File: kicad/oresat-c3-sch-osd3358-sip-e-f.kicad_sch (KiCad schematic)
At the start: 5 parts, among them U1 OSD3358-512M-BSM

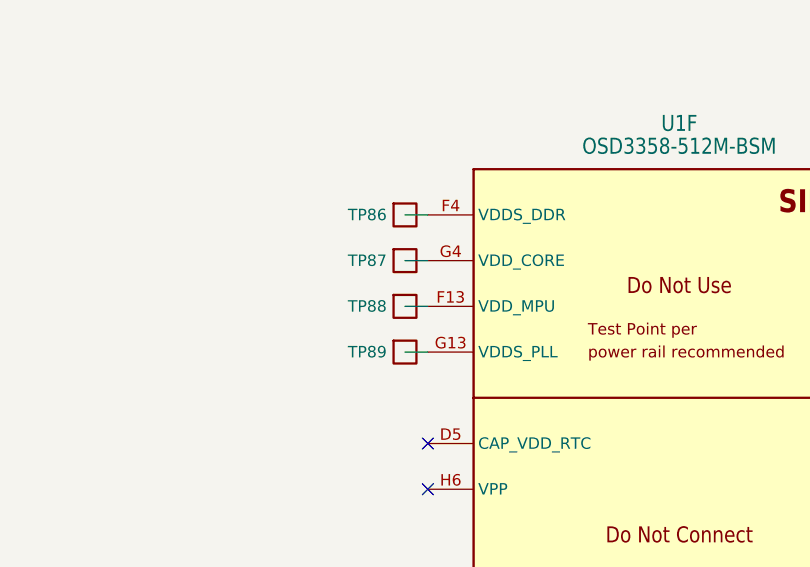
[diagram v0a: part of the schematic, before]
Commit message: Sane amount of ERC errors now; mostly library cleanups.
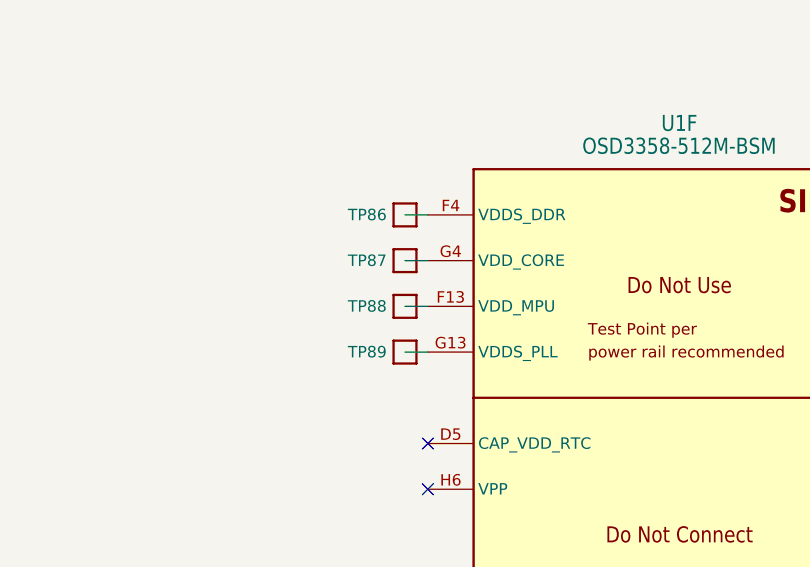
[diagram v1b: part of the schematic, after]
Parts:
- TP86, TP87, TP88, TP89: footprint OreSat-TestPoint:PAD.03X.04 -> oresat-misc:PAD.03X.04; symbol OreSat-TestPoint:Test-Point -> oresat-misc:Test-Point
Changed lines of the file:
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@@
     (effects (font (size 1.27 1.27)) (justify left bottom))
   )
-  (symbol (lib_id "OreSat-Power:GND") (at 250.19 125.73 0) (unit 1)
+  (symbol (lib_id "oresat-power:GND") (at 250.19 125.73 0) (unit 1)
     (in_bom yes) (on_board yes) (dnp no)
     (property "Reference" "#GND0172" (at 250.19 132.08 0)
@@
     )
   )
-  (symbol (lib_id "OreSat-Power:GND") (at 184.15 125.73 0) (unit 1)
+  (symbol (lib_id "oresat-power:GND") (at 184.15 125.73 0) (unit 1)
     (in_bom yes) (on_board yes) (dnp no)
     (property "Reference" "#GND0173" (at 184.15 132.08 0)
@@
     )
   )
-  (symbol (lib_id "OreSat-TestPoint:Test-Point") (at 187.96 162.56 0) (unit 1)
+  (symbol (lib_id "oresat-misc:Test-Point") (at 187.96 162.56 0) (unit 1)
     (in_bom yes) (on_board yes) (dnp no)
     (property "Reference" "TP86" (at 181.61 162.56 0)
@@
       (effects (font (size 1.27 1.27)) hide)
     )
-    (property "Footprint" "OreSat-TestPoint:PAD.03X.04" (at 187.96 160.02 0)
+    (property "Footprint" "oresat-misc:PAD.03X.04" (at 187.96 160.02 0)
       (effects (font (size 1.27 1.27)) hide)
     )
@@
     )
   )
-  (symbol (lib_id "OreSat-TestPoint:Test-Point") (at 187.96 167.64 0) (unit 1)
+  (symbol (lib_id "oresat-misc:Test-Point") (at 187.96 167.64 0) (unit 1)
     (in_bom yes) (on_board yes) (dnp no)
     (property "Reference" "TP87" (at 181.61 167.64 0)
@@
       (effects (font (size 1.27 1.27)) hide)
     )
-    (property "Footprint" "OreSat-TestPoint:PAD.03X.04" (at 187.96 165.1 0)
+    (property "Footprint" "oresat-misc:PAD.03X.04" (at 187.96 165.1 0)
       (effects (font (size 1.27 1.27)) hide)
     )
@@
     )
   )
-  (symbol (lib_id "OreSat-TestPoint:Test-Point") (at 187.96 177.8 0) (unit 1)
+  (symbol (lib_id "oresat-misc:Test-Point") (at 187.96 177.8 0) (unit 1)
     (in_bom yes) (on_board yes) (dnp no)
     (property "Reference" "TP89" (at 181.61 177.8 0)
@@
       (effects (font (size 1.27 1.27)) hide)
     )
-    (property "Footprint" "OreSat-TestPoint:PAD.03X.04" (at 187.96 175.26 0)
+    (property "Footprint" "oresat-misc:PAD.03X.04" (at 187.96 175.26 0)
       (effects (font (size 1.27 1.27)) hide)
     )
@@
     )
   )
-  (symbol (lib_id "OreSat-TestPoint:Test-Point") (at 187.96 172.72 0) (unit 1)
+  (symbol (lib_id "oresat-misc:Test-Point") (at 187.96 172.72 0) (unit 1)
     (in_bom yes) (on_board yes) (dnp no)
     (property "Reference" "TP88" (at 181.61 172.72 0)
@@
       (effects (font (size 1.27 1.27)) hide)
     )
-    (property "Footprint" "OreSat-TestPoint:PAD.03X.04" (at 187.96 170.18 0)
-      (effects (font (size 1.27 1.27)) hide)
-    )
+    (property "Footprint" "oresat-misc:PAD.03X.04" (at 187.96 170.18 0)
+      (effects (font (size 1.27 1.27)) hide)
+    )

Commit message: Big C3 cleanup with Glenn; radios off of one SPS + separate LDOs, removed lots of test 0 ohm resistors, cleaned up capacitance, and finally wired everything up to the octavo. ZERO ERC errors.
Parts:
- TP86, TP87, TP88, TP89: footprint oresat-misc:PAD.03X.04 -> TestPoint:TestPoint_Pad_D1.0mm; symbol oresat-misc:Test-Point -> oresat-misc:Test-Point-1mm-round
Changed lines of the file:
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@@
     )
   )
-  (symbol (lib_id "oresat-misc:Test-Point") (at 187.96 162.56 0) (unit 1)
+  (symbol (lib_id "oresat-misc:Test-Point-1mm-round") (at 187.96 162.56 0) (unit 1)
     (in_bom yes) (on_board yes) (dnp no)
     (property "Reference" "TP86" (at 181.61 162.56 0)
@@
       (effects (font (size 1.27 1.27)) hide)
     )
-    (property "Footprint" "oresat-misc:PAD.03X.04" (at 187.96 160.02 0)
+    (property "Footprint" "TestPoint:TestPoint_Pad_D1.0mm" (at 187.96 152.4 0)
       (effects (font (size 1.27 1.27)) hide)
     )
-    (property "Datasheet" "" (at 187.96 160.02 0)
+    (property "Datasheet" "" (at 187.96 162.56 0)
       (effects (font (size 1.27 1.27)) hide)
     )
@@
     )
   )
-  (symbol (lib_id "oresat-misc:Test-Point") (at 187.96 167.64 0) (unit 1)
+  (symbol (lib_id "oresat-misc:Test-Point-1mm-round") (at 187.96 167.64 0) (unit 1)
     (in_bom yes) (on_board yes) (dnp no)
     (property "Reference" "TP87" (at 181.61 167.64 0)
@@
       (effects (font (size 1.27 1.27)) hide)
     )
-    (property "Footprint" "oresat-misc:PAD.03X.04" (at 187.96 165.1 0)
+    (property "Footprint" "TestPoint:TestPoint_Pad_D1.0mm" (at 187.96 157.48 0)
       (effects (font (size 1.27 1.27)) hide)
     )
-    (property "Datasheet" "" (at 187.96 165.1 0)
+    (property "Datasheet" "" (at 187.96 167.64 0)
       (effects (font (size 1.27 1.27)) hide)
     )
@@
     )
   )
-  (symbol (lib_id "oresat-misc:Test-Point") (at 187.96 177.8 0) (unit 1)
+  (symbol (lib_id "oresat-misc:Test-Point-1mm-round") (at 187.96 177.8 0) (unit 1)
     (in_bom yes) (on_board yes) (dnp no)
     (property "Reference" "TP89" (at 181.61 177.8 0)
@@
       (effects (font (size 1.27 1.27)) hide)
     )
-    (property "Footprint" "oresat-misc:PAD.03X.04" (at 187.96 175.26 0)
+    (property "Footprint" "TestPoint:TestPoint_Pad_D1.0mm" (at 187.96 167.64 0)
       (effects (font (size 1.27 1.27)) hide)
     )
-    (property "Datasheet" "" (at 187.96 175.26 0)
+    (property "Datasheet" "" (at 187.96 177.8 0)
       (effects (font (size 1.27 1.27)) hide)
     )
@@
     )
   )
-  (symbol (lib_id "oresat-misc:Test-Point") (at 187.96 172.72 0) (unit 1)
+  (symbol (lib_id "oresat-misc:Test-Point-1mm-round") (at 187.96 172.72 0) (unit 1)
     (in_bom yes) (on_board yes) (dnp no)
     (property "Reference" "TP88" (at 181.61 172.72 0)
@@
       (effects (font (size 1.27 1.27)) hide)
     )
-    (property "Footprint" "oresat-misc:PAD.03X.04" (at 187.96 170.18 0)
+    (property "Footprint" "TestPoint:TestPoint_Pad_D1.0mm" (at 187.96 162.56 0)
       (effects (font (size 1.27 1.27)) hide)
     )
-    (property "Datasheet" "" (at 187.96 170.18 0)
+    (property "Datasheet" "" (at 187.96 172.72 0)
       (effects (font (size 1.27 1.27)) hide)
     )

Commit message: Fixed test points; added RF test points. Started on layout and component packages for UHF radio.
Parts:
- TP86, TP87, TP88, TP89: footprint TestPoint:TestPoint_Pad_D1.0mm -> oresat-misc:TestPoint_Pad_D1.0mm
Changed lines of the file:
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@@
       (effects (font (size 1.27 1.27)) hide)
     )
-    (property "Footprint" "TestPoint:TestPoint_Pad_D1.0mm" (at 187.96 152.4 0)
+    (property "Footprint" "oresat-misc:TestPoint_Pad_D1.0mm" (at 187.96 152.4 0)
       (effects (font (size 1.27 1.27)) hide)
     )
@@
       (effects (font (size 1.27 1.27)) hide)
     )
-    (property "Footprint" "TestPoint:TestPoint_Pad_D1.0mm" (at 187.96 157.48 0)
+    (property "Footprint" "oresat-misc:TestPoint_Pad_D1.0mm" (at 187.96 157.48 0)
       (effects (font (size 1.27 1.27)) hide)
     )
@@
       (effects (font (size 1.27 1.27)) hide)
     )
-    (property "Footprint" "TestPoint:TestPoint_Pad_D1.0mm" (at 187.96 167.64 0)
+    (property "Footprint" "oresat-misc:TestPoint_Pad_D1.0mm" (at 187.96 167.64 0)
       (effects (font (size 1.27 1.27)) hide)
     )
@@
       (effects (font (size 1.27 1.27)) hide)
     )
-    (property "Footprint" "TestPoint:TestPoint_Pad_D1.0mm" (at 187.96 162.56 0)
+    (property "Footprint" "oresat-misc:TestPoint_Pad_D1.0mm" (at 187.96 162.56 0)
       (effects (font (size 1.27 1.27)) hide)
     )

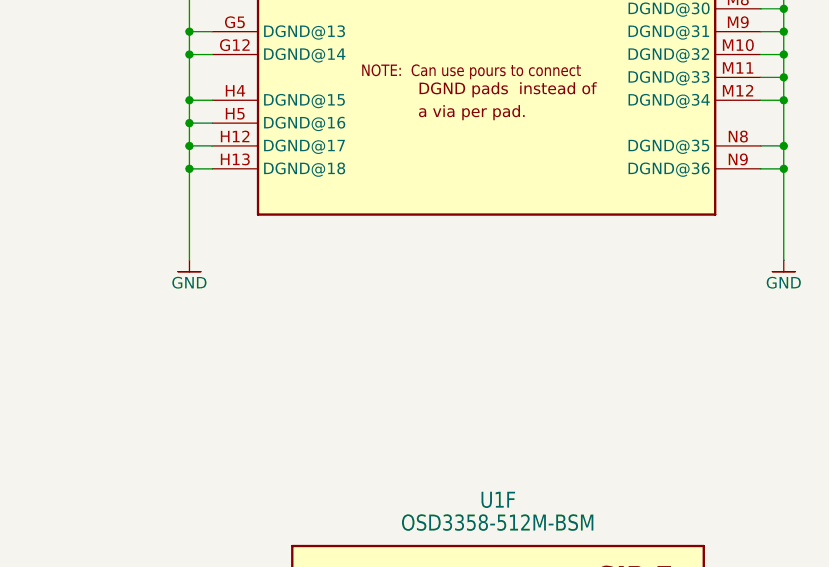
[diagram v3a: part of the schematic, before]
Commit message: Fixed footprints and laid out WDT and OPD circuitry.
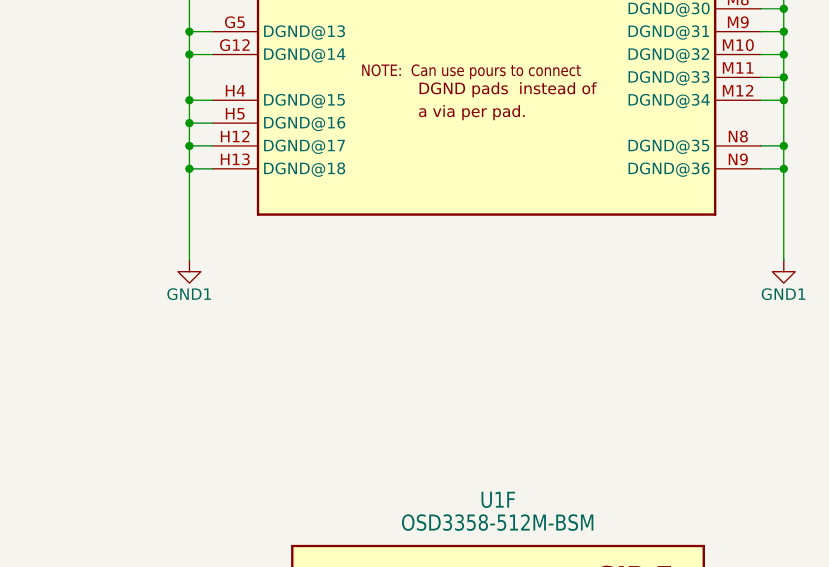
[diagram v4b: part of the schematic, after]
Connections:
- net GND renamed GND1
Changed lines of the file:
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@@
     (effects (font (size 1.27 1.27)) (justify left bottom))
   )
-  (symbol (lib_id "oresat-power:GND") (at 250.19 125.73 0) (unit 1)
+  (symbol (lib_id "power:GND1") (at 250.19 125.73 0) (unit 1)
     (in_bom yes) (on_board yes) (dnp no)
     (property "Reference" "#GND0172" (at 250.19 132.08 0)
       (effects (font (size 1.27 1.27)) hide)
     )
-    (property "Value" "GND" (at 250.19 128.27 0)
+    (property "Value" "GND1" (at 250.19 129.54 0)
       (effects (font (size 1.27 1.27)))
     )
@@
         )
         (path "/65d12cdd-c326-4033-9053-c59fa4e0b25e/ce2d6150-524f-4c6f-aba3-da83a5df548c"
-          (reference "#GND036") (unit 1)
+          (reference "#PWR0161") (unit 1)
         )
       )
     )
   )
-  (symbol (lib_id "oresat-power:GND") (at 184.15 125.73 0) (unit 1)
+  (symbol (lib_id "power:GND1") (at 184.15 125.73 0) (unit 1)
     (in_bom yes) (on_board yes) (dnp no)
     (property "Reference" "#GND0173" (at 184.15 132.08 0)
       (effects (font (size 1.27 1.27)) hide)
     )
-    (property "Value" "GND" (at 184.15 128.27 0)
+    (property "Value" "GND1" (at 184.15 129.54 0)
       (effects (font (size 1.27 1.27)))
     )
@@
         )
         (path "/65d12cdd-c326-4033-9053-c59fa4e0b25e/ce2d6150-524f-4c6f-aba3-da83a5df548c"
-          (reference "#GND035") (unit 1)
+          (reference "#PWR0160") (unit 1)
         )
       )

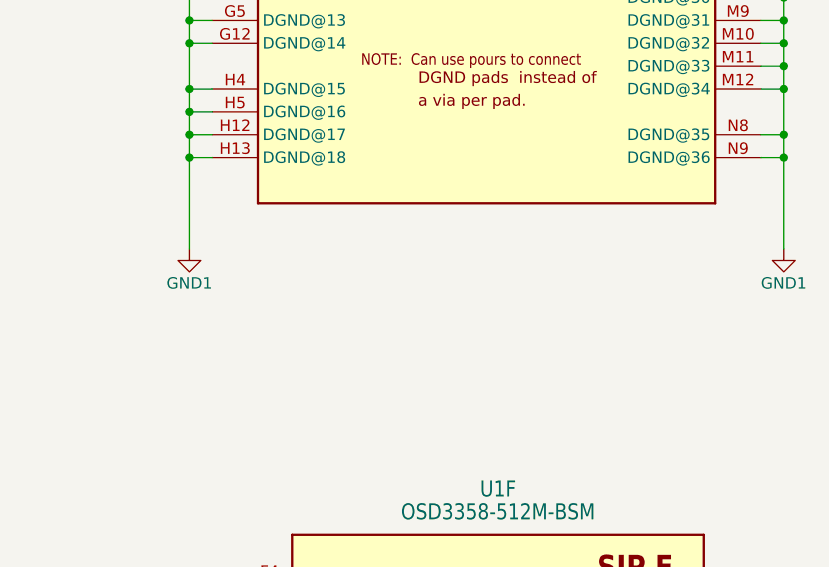
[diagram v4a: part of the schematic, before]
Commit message: Switched all grounds to a single ground, because I can't find a way to overlap ground planes in KiCAD. That's actually not terrible, however, because KiCAD has an anti-plane feature which I used to cut the ground plane between UHF and L radios and L radio and Octavo. So actually I think it came out better than having separate ground planes. Only thing left now are the ~ 40 connections to the Octavo.
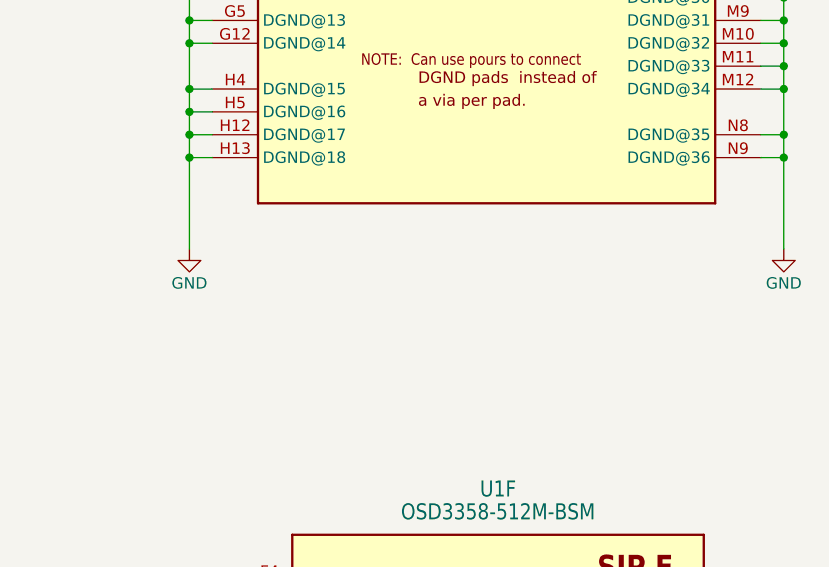
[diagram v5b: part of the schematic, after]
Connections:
- net GND1 renamed GND
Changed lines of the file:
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@@
     (effects (font (size 1.27 1.27)) (justify left bottom))
   )
-  (symbol (lib_id "power:GND1") (at 250.19 125.73 0) (unit 1)
+  (symbol (lib_id "power:GND") (at 250.19 125.73 0) (unit 1)
     (in_bom yes) (on_board yes) (dnp no)
     (property "Reference" "#GND0172" (at 250.19 132.08 0)
       (effects (font (size 1.27 1.27)) hide)
     )
-    (property "Value" "GND1" (at 250.19 129.54 0)
+    (property "Value" "GND" (at 250.19 129.54 0)
       (effects (font (size 1.27 1.27)))
     )
@@
         )
         (path "/65d12cdd-c326-4033-9053-c59fa4e0b25e/ce2d6150-524f-4c6f-aba3-da83a5df548c"
-          (reference "#PWR0161") (unit 1)
+          (reference "#PWR?") (unit 1)
         )
       )
     )
   )
-  (symbol (lib_id "power:GND1") (at 184.15 125.73 0) (unit 1)
+  (symbol (lib_id "power:GND") (at 184.15 125.73 0) (unit 1)
     (in_bom yes) (on_board yes) (dnp no)
     (property "Reference" "#GND0173" (at 184.15 132.08 0)
       (effects (font (size 1.27 1.27)) hide)
     )
-    (property "Value" "GND1" (at 184.15 129.54 0)
+    (property "Value" "GND" (at 184.15 129.54 0)
       (effects (font (size 1.27 1.27)))
     )
@@
         )
         (path "/65d12cdd-c326-4033-9053-c59fa4e0b25e/ce2d6150-524f-4c6f-aba3-da83a5df548c"
-          (reference "#PWR0160") (unit 1)
+          (reference "#PWR?") (unit 1)
         )
       )

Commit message: Last of the ERC and DRC errors! only polishing left.
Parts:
- U1: footprint oresat-footprints:U-Octavo-OSD335X-BGA-256 -> oresat-ics:U-Octavo-OSD335X-BGA-256
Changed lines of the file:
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@@
       (effects (font (size 1.778 1.5113)))
     )
-    (property "Footprint" "oresat-footprints:U-Octavo-OSD335X-BGA-256" (at 218.44 74.93 0)
+    (property "Footprint" "oresat-ics:U-Octavo-OSD335X-BGA-256" (at 218.44 74.93 0)
       (effects (font (size 1.27 1.27)) hide)
     )
@@
       (effects (font (size 1.778 1.5113)))
     )
-    (property "Footprint" "oresat-footprints:U-Octavo-OSD335X-BGA-256" (at 217.17 -20.32 0)
-      (effects (font (size 1.27 1.27)) hide)
-    )
+    (property "Footprint" "oresat-ics:U-Octavo-OSD335X-BGA-256" (at 217.17 -20.32 0)
+      (effects (font (size 1.27 1.27)) hide)
+    )
